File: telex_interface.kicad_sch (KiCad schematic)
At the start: 14 parts, among them J1 DB25_Female_MountingHoles, J2 Conn_01x08, U1 max3387

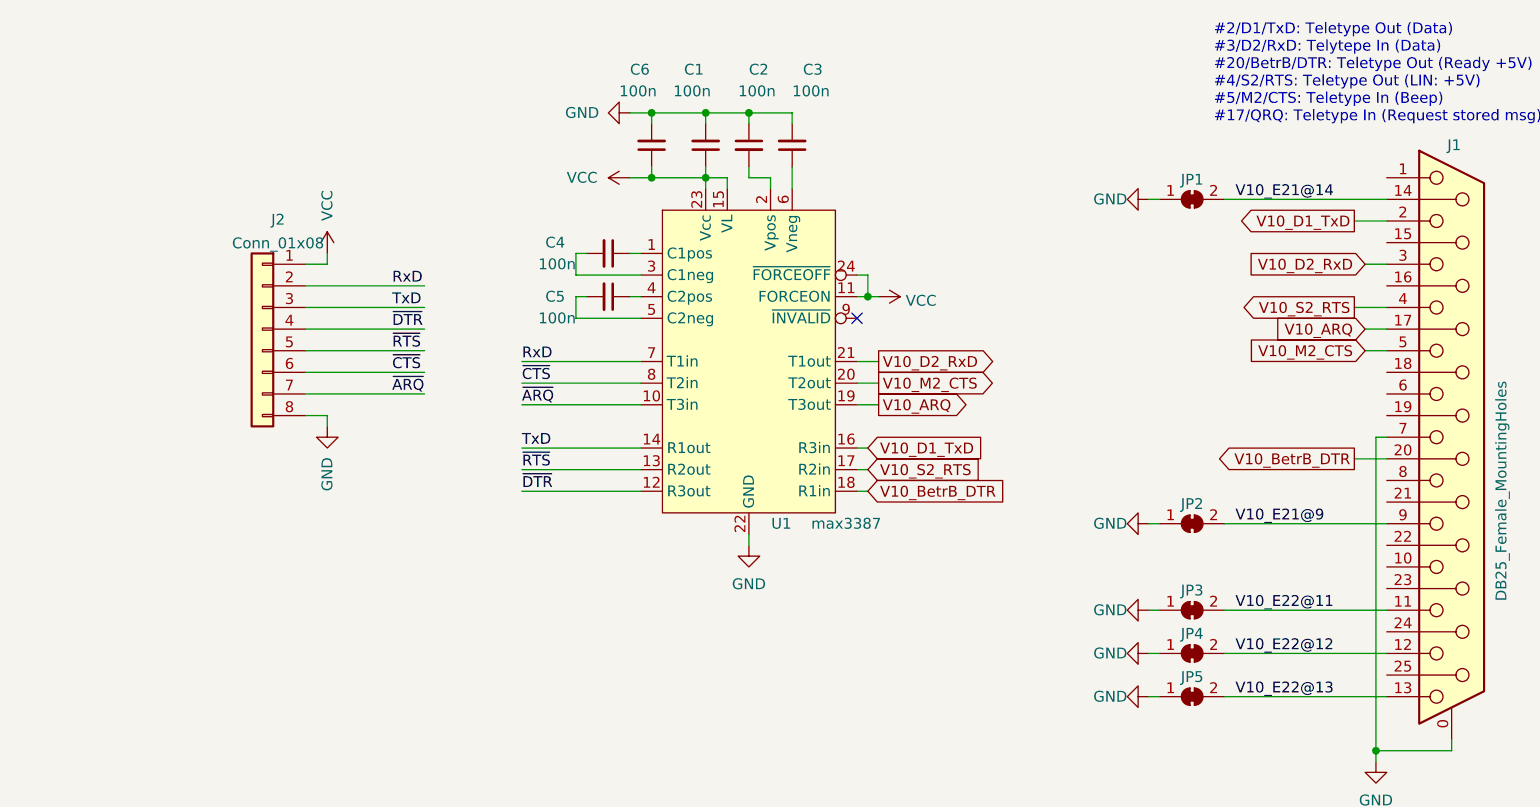
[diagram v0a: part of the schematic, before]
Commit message: NAND gate for half dumplex echo and pullups
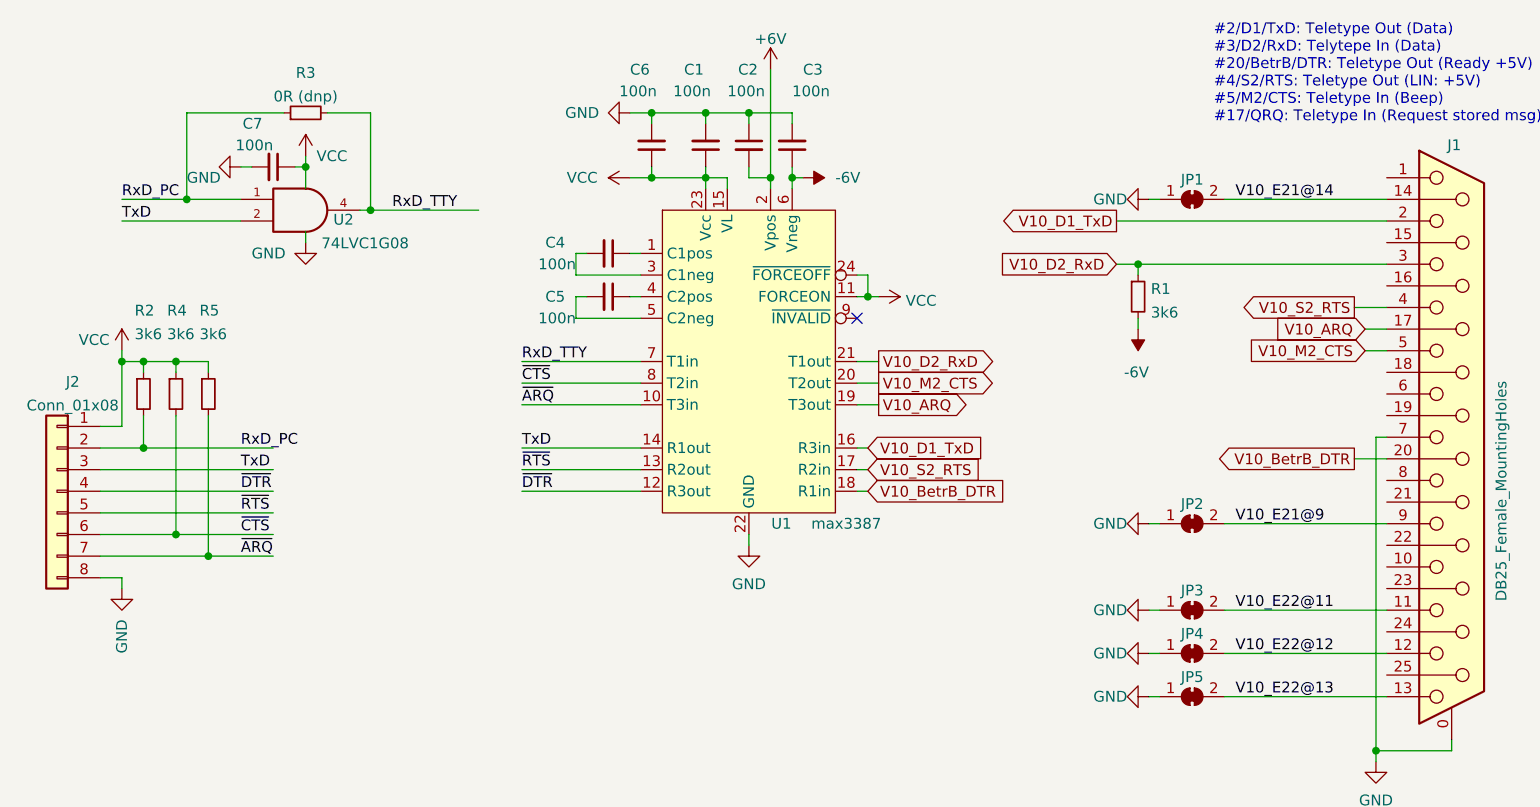
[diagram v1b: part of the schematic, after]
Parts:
- added C7: 100n, Capacitor_SMD:C_0603_1608Metric, symbol Device:C_Small
- added R1, R2, R4, R5: 3k6, Resistor_SMD:R_0603_1608Metric, symbol Device:R_Small
- added R3: 0R (dnp), Resistor_SMD:R_0603_1608Metric, symbol Device:R_Small
- added U2: 74LVC1G08, Package_TO_SOT_SMD:SOT-353_SC-70-5, symbol 74xGxx:74LVC1G08
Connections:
- net GND: now also C7.2, U2.3 (GND)
- net TxD: now also U2.2
- net V10_D2_RxD: now also R1.1
- net VCC: now also C7.1, R2.1, R4.1, R5.1, U2.5 (VCC)
- net ~{ARQ}: now also R5.2
- net ~{CTS}: now also R4.2
- net +6V: now reaches C2.2, U1.2 (Vpos)
- net -6V: now reaches C3.1, U1.6 (Vneg)
- net -6V: now also R1.2
- net RxD renamed RxD_PC
- net RxD_PC: now also R2.2, R3.1, U2.1; no longer U1.7 (T1in)
- new net RxD_TTY: R3.2, U1.7 (T1in), U2.4
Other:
- moved on the sheet: J2

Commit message: more work
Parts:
- removed J2: Conn_01x08, Connector_PinHeader_2.54mm:PinHeader_1x08_P2.54mm_Vertical, symbol Connector_Generic:Conn_01x08
- removed R4, R5: 3k6, Resistor_SMD:R_0603_1608Metric, symbol Device:R_Small
- added C10, C9: 100n, Capacitor_SMD:C_0603_1608Metric, symbol Device:C_Small
- added C8: 10u, Capacitor_SMD:C_0603_1608Metric, symbol Device:C_Small
- added J2: Conn_02x08_Odd_Even, Connector_PinHeader_2.54mm:PinHeader_2x08_P2.54mm_Vertical, symbol Connector_Generic:Conn_02x08_Odd_Even
- added J3: USB_B_Mini, Connector_USB:USB_Mini-B_Wuerth_65100516121_Horizontal, symbol Connector:USB_B_Mini
- added JP6: Jumper_2_Open, Connector_PinHeader_2.54mm:PinHeader_2x01_P2.54mm_Vertical, symbol Jumper:Jumper_2_Open
- added R6: 10k, Resistor_SMD:R_0603_1608Metric, symbol Device:R_Small
- added R7: 22R, Resistor_SMD:R_0603_1608Metric, symbol Device:R_Small
- added U3: CH340G, Package_SO:SOIC-16_3.9x9.9mm_P1.27mm, symbol Interface_USB:CH340G
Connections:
- net GND: now also C10.1, C8.1, C9.2, J2.1 (Pin_1), J2.16 (Pin_16), J3.5 (GND), J3.6 (Shield), U3.1 (GND)
- net RxD_PC: now also J2.4 (Pin_4)
- net TxD: now also J2.6 (Pin_6), R6.1; no longer U2.2
- net VCC: now also C9.1, J2.2 (Pin_2), JP6.2 (B), U3.4 (V3)
- net ~{ARQ}: now also J2.14 (Pin_14)
- net V10_M2_CTS renamed V10_M2
- net ~{CTS} renamed ~{M2}
- net ~{M2}: now also J2.12 (Pin_12)
- net ~{DTR} renamed ~{BetrB_DTR}
- net ~{BetrB_DTR}: now also J2.10 (Pin_10)
- net ~{RTS} renamed ~{S2_RTS}
- net ~{S2_RTS}: now also J2.8 (Pin_8)
- new net: J3.1 (VBUS), R7.1
- new net: JP6.1 (A), R6.2, U2.2
- new net: J3.3 (D+), U3.5 (UD+)
- new net: J3.2 (D-), U3.6 (UD-)
- new net USB_RxD: J2.5 (Pin_5), U3.3 (RXD)
- new net USB_TxD: J2.3 (Pin_3), U3.2 (TXD)
- new net VBUS: C10.2, C8.2, R7.2, U3.16 (VCC)
- new net ~{USB_CTS}: J2.7 (Pin_7), U3.9 (~{CTS})
- new net ~{USB_DCD}: J2.11 (Pin_11), U3.12 (~{DCD})
- new net ~{USB_DSR}: J2.9 (Pin_9), U3.10 (~{DSR})
- new net ~{USB_DTR}: J2.13 (Pin_13), U3.13 (~{DTR})
- new net ~{USB_RTS}: J2.15 (Pin_15), U3.14 (~{RTS})
- no-connect marks 1 -> 14
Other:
- note added: "#2/D1/TxD: Teletype Out (Data) #3/D2/RxD: Telytepe In (Data) #20/BetrB/DTR: Teletype Out (Ready +5V) #4/S2/RTS: Teletype Out (LIN: +5V) #5/M2: Teletype In (Beep) #17/ARQ: Teletype In (Request stored msg)"
- note added: "close jumper to disable echo"
- note removed: "#2/D1/TxD: Teletype Out (Data) #3/D2/RxD: Telytepe In (Data) #20/BetrB/DTR: Teletype Out (Ready +5V) #4/S2/RTS: Teletype Out (LIN: +5V) #5/M2/CTS: Teletype In (Beep) #17/QRQ: Teletype In (Request stored msg)"
- moved on the sheet: C1, C2, C3, C4, C5, C6, C7, R2, R3, U1, U2

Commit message: add power led
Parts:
- added D1: LED, LED_SMD:LED_0603_1608Metric, symbol Device:LED
- added R4: 22R, Resistor_SMD:R_0603_1608Metric, symbol Device:R_Small
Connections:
- net GND: now also D1.1 (K)
- net VCC: now also R4.2
- new net: D1.2 (A), R4.1

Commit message: more work
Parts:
- added C11, C12: 22p, Capacitor_SMD:C_0603_1608Metric, symbol Device:C_Small
- added H1, H2: MountingHole_Pad, MountingHole:MountingHole_3.2mm_M3_DIN965_Pad, symbol Mechanical:MountingHole_Pad
- added JP7: SolderJumper_2_Bridged, Jumper:SolderJumper-2_P1.3mm_Bridged_Pad1.0x1.5mm, symbol Jumper:SolderJumper_2_Bridged
- added TP1, TP10, TP11, TP12, TP13, TP2, TP3, TP4, TP5, TP6, TP7, TP8, TP9: TestPoint, TestPoint:TestPoint_Pad_2.0x2.0mm, symbol Connector:TestPoint
- added Y1: EuroQuartz MJ 5x3.2mm 12MHz, Crystal:Crystal_SMD_EuroQuartz_MJ-4Pin_5.0x3.2mm_HandSoldering, symbol Device:Crystal_GND24_Small
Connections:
- net +6V: now also TP7.1
- net -6V: now also TP8.1
- net GND: now also C11.2, C12.2, H1.1, H2.1, JP7.1 (A), TP10.1, TP11.1, TP12.1, Y1.2, Y1.4
- net V10_ARQ: now also TP3.1
- net V10_BetrB_DTR: now also TP6.1
- net V10_D1_TxD: now also TP4.1
- net V10_D2_RxD: now also TP1.1
- net V10_M2: now also TP2.1
- net V10_S2_RTS: now also TP5.1
- net VCC: now also TP13.1, TP9.1
- net SHIELD@1: now reaches J1.1
- net SHIELD@1: now also JP7.2 (B)
- net USB_DP: now reaches J3.3 (D+), U3.5 (UD+)
- net USB_DN: now reaches J3.2 (D-), U3.6 (UD-)
- net at U3.7 (XI): now also C11.1, Y1.1
- net at U3.8 (XO): now also C12.1, Y1.3
- no-connect marks 14 -> 13

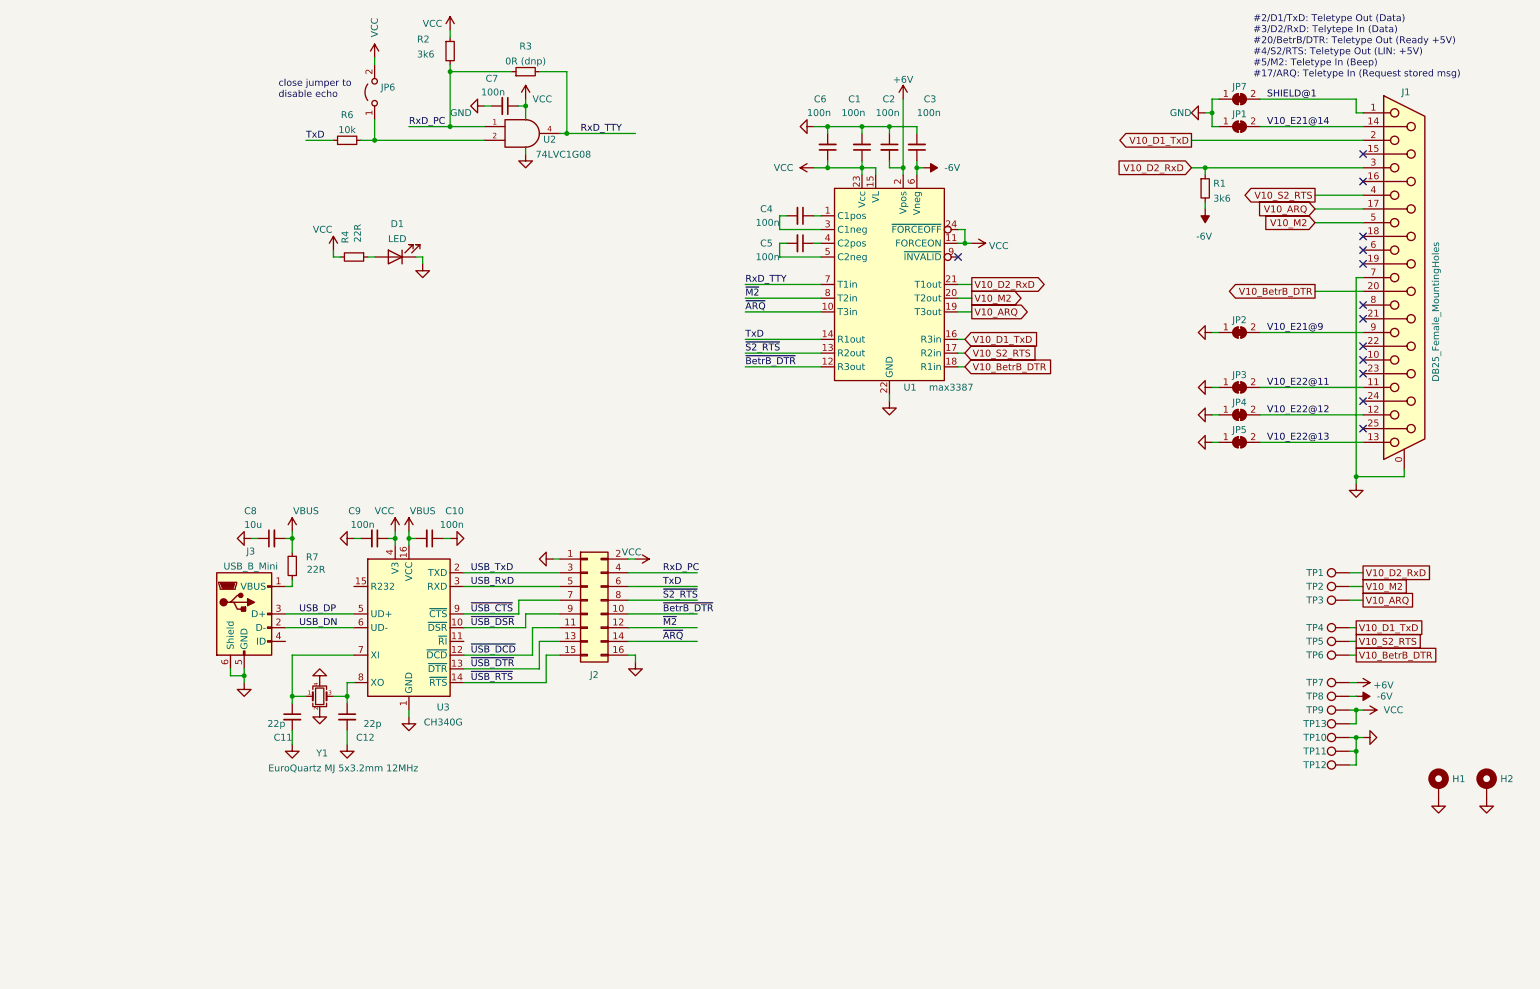
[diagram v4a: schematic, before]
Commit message: Add Raspi header.
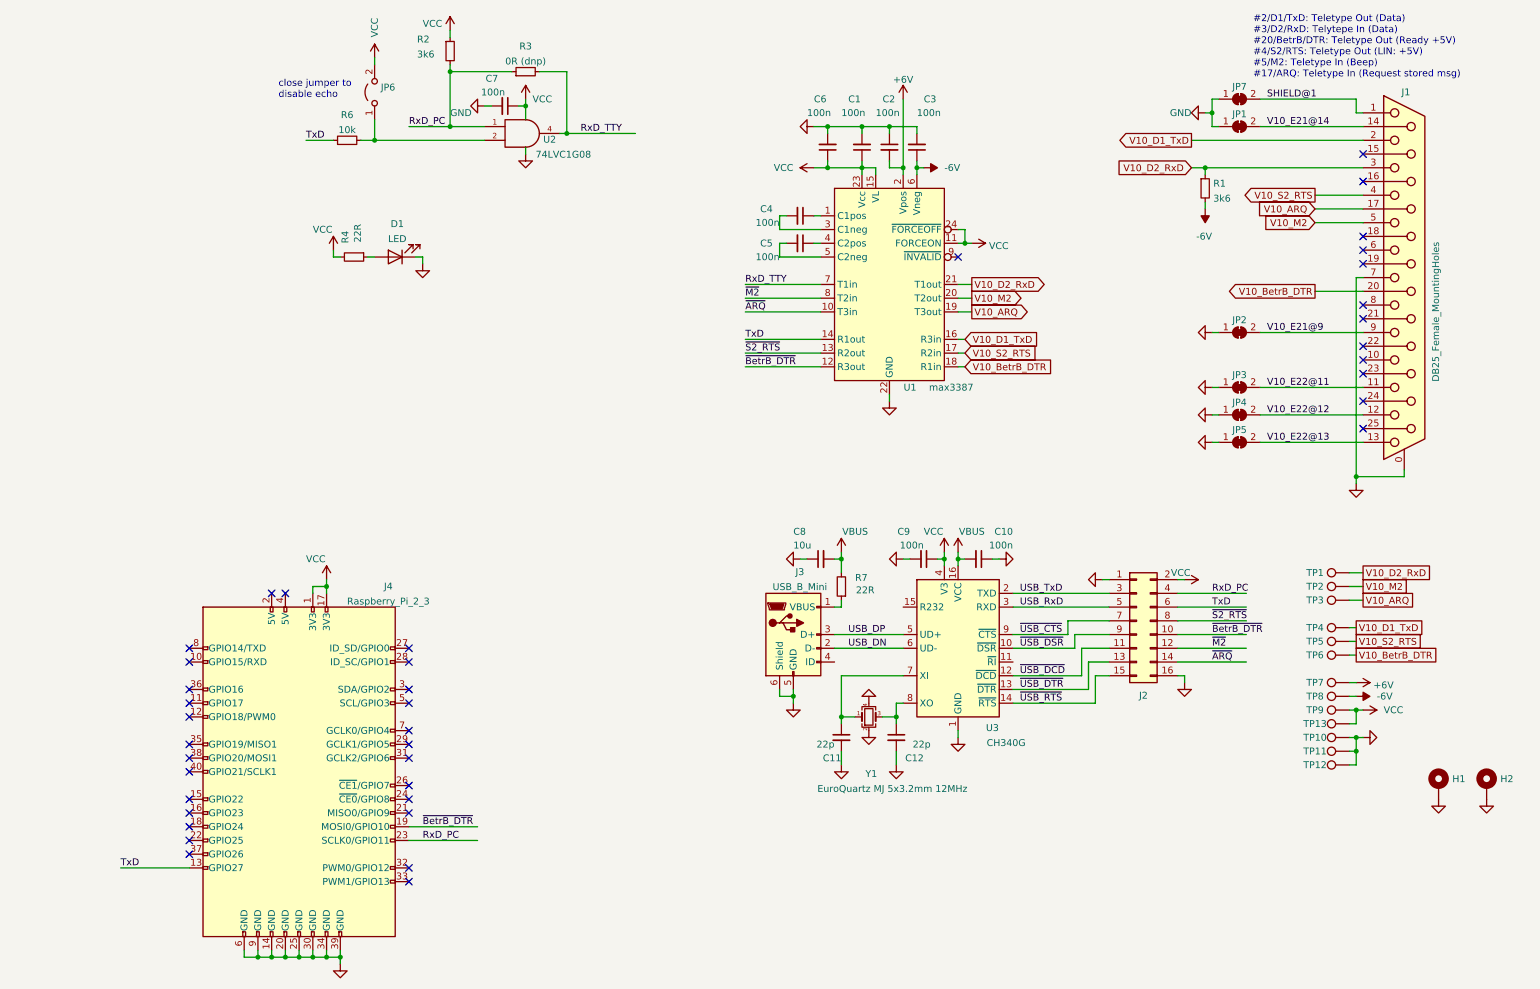
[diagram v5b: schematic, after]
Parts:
- added J4: Raspberry_Pi_2_3, Connector_PinSocket_2.54mm:PinSocket_2x20_P2.54mm_Vertical, symbol Connector:Raspberry_Pi_2_3
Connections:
- net GND: now also J4.14 (GND), J4.20 (GND), J4.25 (GND), J4.30 (GND), J4.34 (GND), J4.39 (GND), J4.6 (GND), J4.9 (GND)
- net RxD_PC: now also J4.23 (SCLK0/GPIO11)
- net TxD: now also J4.13 (GPIO27)
- net VCC: now also J4.1 (3V3), J4.17 (3V3)
- net ~{BetrB_DTR}: now also J4.19 (MOSI0/GPIO10)
- no-connect marks 13 -> 40
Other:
- moved on the sheet: C10, C11, C12, C8, C9, J2, J3, R7, U3, Y1

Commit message: removed USB again, made smaller
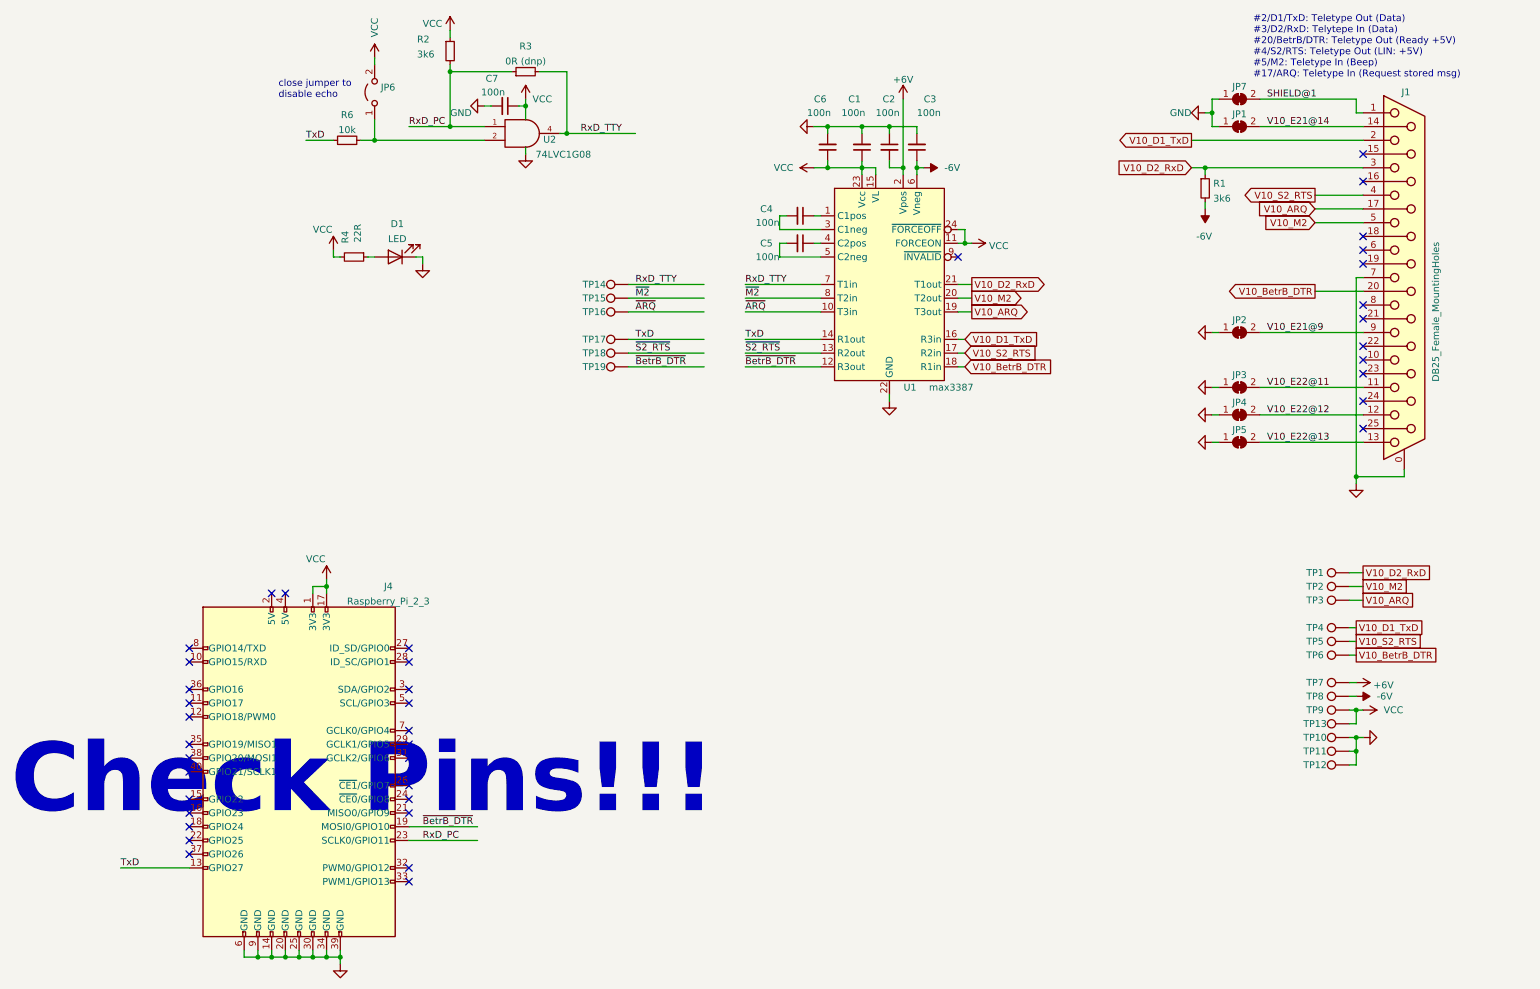
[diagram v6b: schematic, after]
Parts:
- removed C10, C9: 100n, Capacitor_SMD:C_0603_1608Metric, symbol Device:C_Small
- removed C11, C12: 22p, Capacitor_SMD:C_0603_1608Metric, symbol Device:C_Small
- removed C8: 10u, Capacitor_SMD:C_0603_1608Metric, symbol Device:C_Small
- removed H1, H2: MountingHole_Pad, MountingHole:MountingHole_3.2mm_M3_DIN965_Pad, symbol Mechanical:MountingHole_Pad
- removed J2: Conn_02x08_Odd_Even, Connector_PinHeader_2.54mm:PinHeader_2x08_P2.54mm_Vertical, symbol Connector_Generic:Conn_02x08_Odd_Even
- removed J3: USB_B_Mini, Connector_USB:USB_Mini-B_Wuerth_65100516121_Horizontal, symbol Connector:USB_B_Mini
- removed R7: 22R, Resistor_SMD:R_0603_1608Metric, symbol Device:R_Small
- removed U3: CH340G, Package_SO:SOIC-16_3.9x9.9mm_P1.27mm, symbol Interface_USB:CH340G
- removed Y1: EuroQuartz MJ 5x3.2mm 12MHz, Crystal:Crystal_SMD_EuroQuartz_MJ-4Pin_5.0x3.2mm_HandSoldering, symbol Device:Crystal_GND24_Small
- added TP14, TP15, TP16, TP17, TP18, TP19: TestPoint, TestPoint:TestPoint_Pad_2.0x2.0mm, symbol Connector:TestPoint
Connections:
- net RxD_TTY: now also TP14.1
- net TxD: now also TP17.1
- net ~{ARQ}: now also TP16.1
- net ~{BetrB_DTR}: now also TP19.1
- net ~{M2}: now also TP15.1
- net ~{S2_RTS}: now also TP18.1
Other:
- note added: "Check Pins!!!"
